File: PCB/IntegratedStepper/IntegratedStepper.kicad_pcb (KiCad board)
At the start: 4 copper layers, 42 x 49.8 mm, 75 parts, among them IC2 SN65HVD230DR, IC3 LMR38020FSQDDARQ1, J3 Screw_Terminal_01x02, J4 Screw_Terminal_01x02, J5 Conn_01x05_Socket, Q1 SS8050-G, Q2 SS8050-G, U1 ESP32-WROOM-32E, U2 AS5048A, U3 CP2102N-Axx-xQFN28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

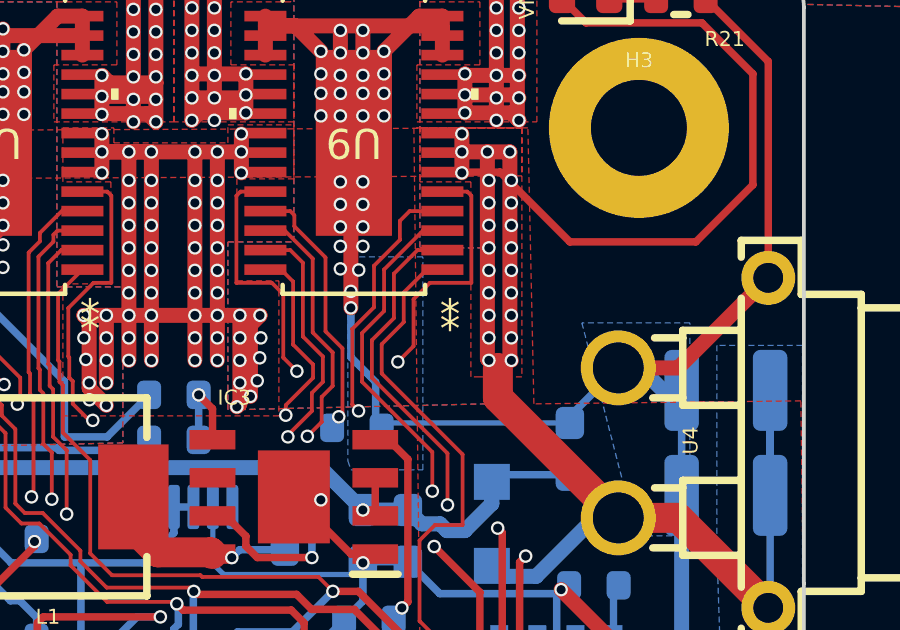
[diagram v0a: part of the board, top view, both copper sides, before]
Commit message: Create initial driver for DRV824x drivers for ESP32 / SimpleFOC
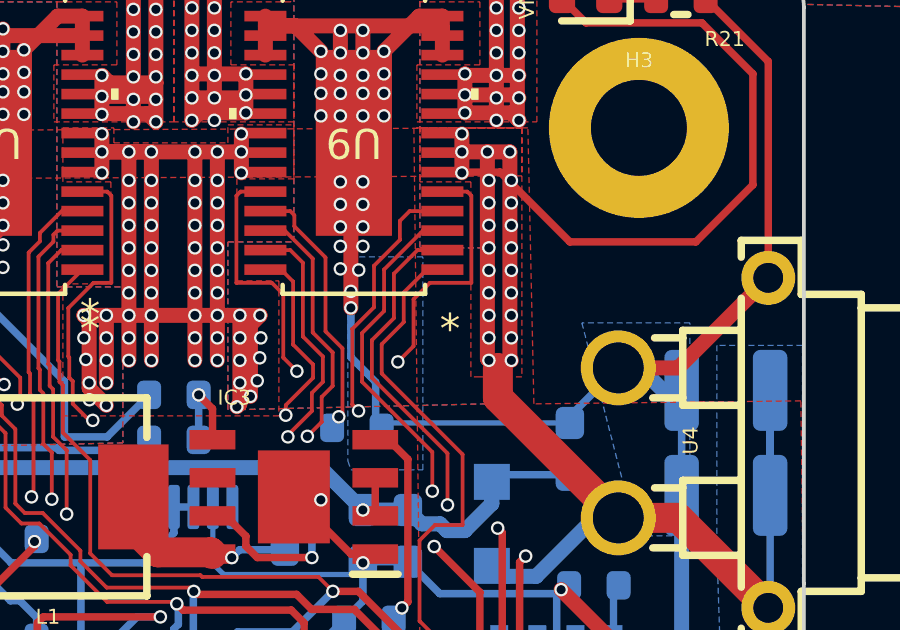
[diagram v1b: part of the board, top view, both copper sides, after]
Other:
- copper layers 4 -> 6
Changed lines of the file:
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@@
 		(1 "In1.Cu" signal)
 		(2 "In2.Cu" signal)
+		(3 "In3.Cu" signal)
+		(4 "In4.Cu" signal)
 		(31 "B.Cu" signal)
 		(32 "B.Adhes" user "B.Adhesive")
@@
 			(layer "dielectric 2"
 				(type "core")
-				(thickness 1.24)
+				(thickness 0.535)
 				(material "FR4")
 				(epsilon_r 4.5)
@@
 				(loss_tangent 0.02)
 			)
+			(layer "In3.Cu"
+				(type "copper")
+				(thickness 0.035)
+			)
+			(layer "dielectric 4"
+				(type "core")
+				(thickness 0.535)
+				(material "FR4")
+				(epsilon_r 4.5)
+				(loss_tangent 0.02)
+			)
+			(layer "In4.Cu"
+				(type "copper")
+				(thickness 0.035)
+			)
+			(layer "dielectric 5"
+				(type "prepreg")
+				(thickness 0.1)
+				(material "FR4")
+				(epsilon_r 4.5)
+				(loss_tangent 0.02)
+			)
 			(layer "B.Cu"
 				(type "copper")
@@
 			(size 6 6)
 			(drill 3.2)
-			(layers "F&B.Cu" "*.Mask")
+			(layers "*.Cu" "*.Mask")
 		)
 	)
@@
 			)
 		)
-		(property "Footprint" "U_PWP0028R_TEX"
+		(property "Footprint" "PDRV8245SPWPQ1:U_PWP0028R_TEX"
 			(at 0 0 180)
 			(unlocked yes)
@@
 		(fp_text user "*"
 			(at -1.8669 -4.826 180)
+			(unlocked yes)
 			(layer "F.Fab")
 			(effects
@@
 			(pintype "power_out")
 		)
+		(model "D:/GitHub/PersonalProjects/KiCad Libraries/TI_Libraries/TI_3DModels/PWP0028R.stp"
+			(offset
+				(xyz 0 0 0)
+			)
+			(scale
+				(xyz 1 1 1)
+			)
+			(rotate
+				(xyz 0 0 0)
+			)
+		)
 	)
 	(footprint "MountingHole:MountingHole_3.2mm_M3"
@@
 			(size 6 6)
 			(drill 3.2)
-			(layers "F&B.Cu" "*.Mask")
+			(layers "*.Cu" "*.Mask")
 		)
 	)
@@
 			)
 		)
-		(property "Footprint" "U_PWP0028R_TEX"
+		(property "Footprint" "PDRV8245SPWPQ1:U_PWP0028R_TEX"
 			(at 0 0 180)
 			(unlocked yes)
@@
 		(fp_text user "*"
 			(at -3.20395 -5.7228 180)
+			(unlocked yes)
 			(layer "F.SilkS")
 			(effects
@@
 			)
 		)
-		(fp_text user "*"
-			(at -1.8669 -4.826 180)
+		(fp_text user "${REFERENCE}"
+			(at 0 0 180)
+			(unlocked yes)
 			(layer "F.Fab")
 			(effects
@@
 			)
 		)
-		(fp_text user "${REFERENCE}"
-			(at 0 0 180)
-			(unlocked yes)
+		(fp_text user "*"
+			(at -1.8669 -4.826 180)
 			(layer "F.Fab")
 			(effects
@@
 			(pintype "power_out")
 		)
+		(model "D:/GitHub/PersonalProjects/KiCad Libraries/TI_Libraries/TI_3DModels/PWP0028R.stp"
+			(offset
+				(xyz 0 0 0)
+			)
+			(scale
+				(xyz 1 1 1)
+			)
+			(rotate
+				(xyz 0 0 0)
+			)
+		)
 	)
